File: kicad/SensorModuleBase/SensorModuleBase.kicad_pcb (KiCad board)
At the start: 2 copper layers, 59 x 57 mm, 6 parts, among them J1 Conn_02x08_Top_Bottom, U1 AT28C64B-15PU, U2 74HC00, U3 SN74HC595N, U4 SN74HC595N

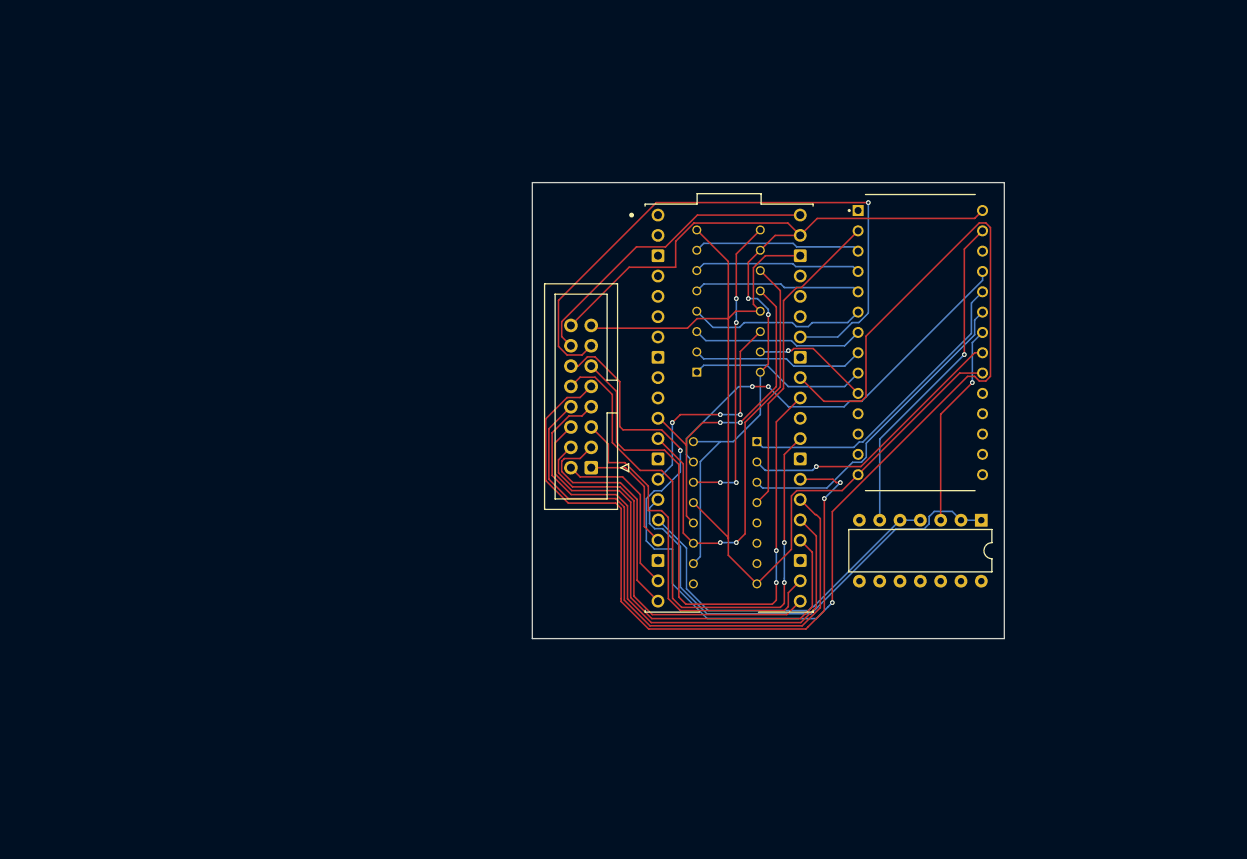
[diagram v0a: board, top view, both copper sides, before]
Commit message: added some kicad files and fixed circuit
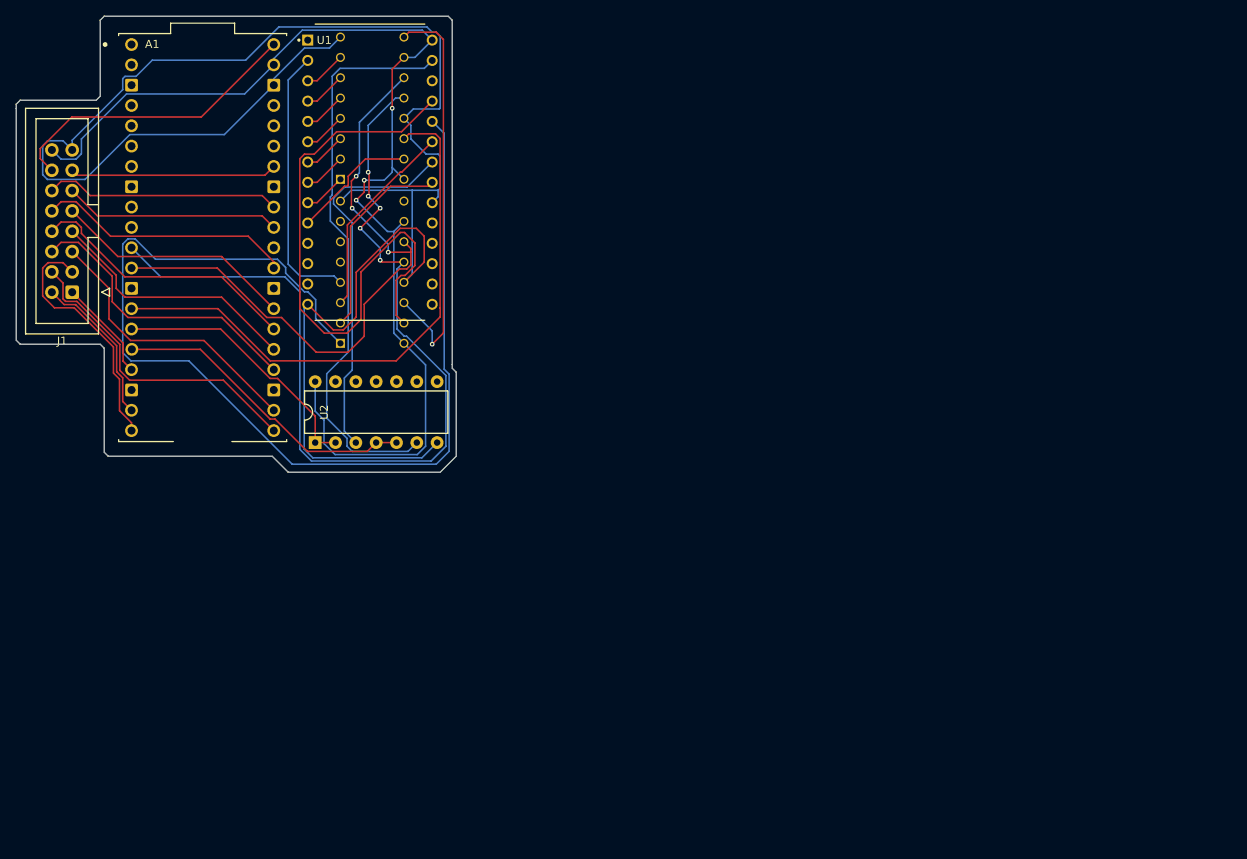
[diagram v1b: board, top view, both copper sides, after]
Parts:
- moved U2 83.8 mm to (52.9, 67.5), turned to 90 degrees
- moved U1 72.0 mm to (59.7, 33.7)
- moved A1 69.2 mm to (38.8, 41.9)
- moved J1 68.5 mm to (22.5, 48.7)
- moved U4 53.4 mm to (60.0, 46.2), turned to 0 degrees
- moved U3 50.7 mm to (60.0, 25.7)
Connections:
- U2 pad 14: (no net) -> Net-(A1-VSYS)
- U2 pad 7: (no net) -> Net-(J1-Pin_15)
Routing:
- net Net-(A1-GP27): track 162.8 -> 29.5 mm, vias 2 -> 0
- net Net-(U1-A9): track 38.8 -> 137.6 mm
- net Net-(J1-Pin_15): track 131.1 -> 228.3 mm
- net Net-(A1-GP8): track 42.6 -> 117.3 mm, vias 2 -> 5
- net Net-(A1-GP21): track 87.4 -> 30.3 mm, vias 2 -> 0
- net Net-(A1-GP28): track 78.1 -> 25.9 mm, vias 1 -> 0
- net Net-(A1-GP26): track 75.6 -> 27.1 mm, vias 2 -> 0
- net Net-(A1-GP10): track 28.2 -> 70.9 mm, vias 3 -> 0
- net Net-(A1-GP22): track 72.8 -> 32.1 mm, vias 2 -> 0
- net Net-(A1-GP20): track 74.1 -> 34.2 mm
- net Net-(A1-GP19): track 71.6 -> 32.3 mm
- net Net-(U1-~{WE}): track 41.5 -> 72.2 mm, vias 1 -> 0
- net Net-(A1-VSYS): track 116.0 -> 143.5 mm, vias 2 -> 3
- net Net-(A1-GP18): track 62.8 -> 36.7 mm
- net Net-(A1-GP11): track 58.9 -> 33.3 mm
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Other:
- board size 59 x 57 mm -> 55 x 57 mm

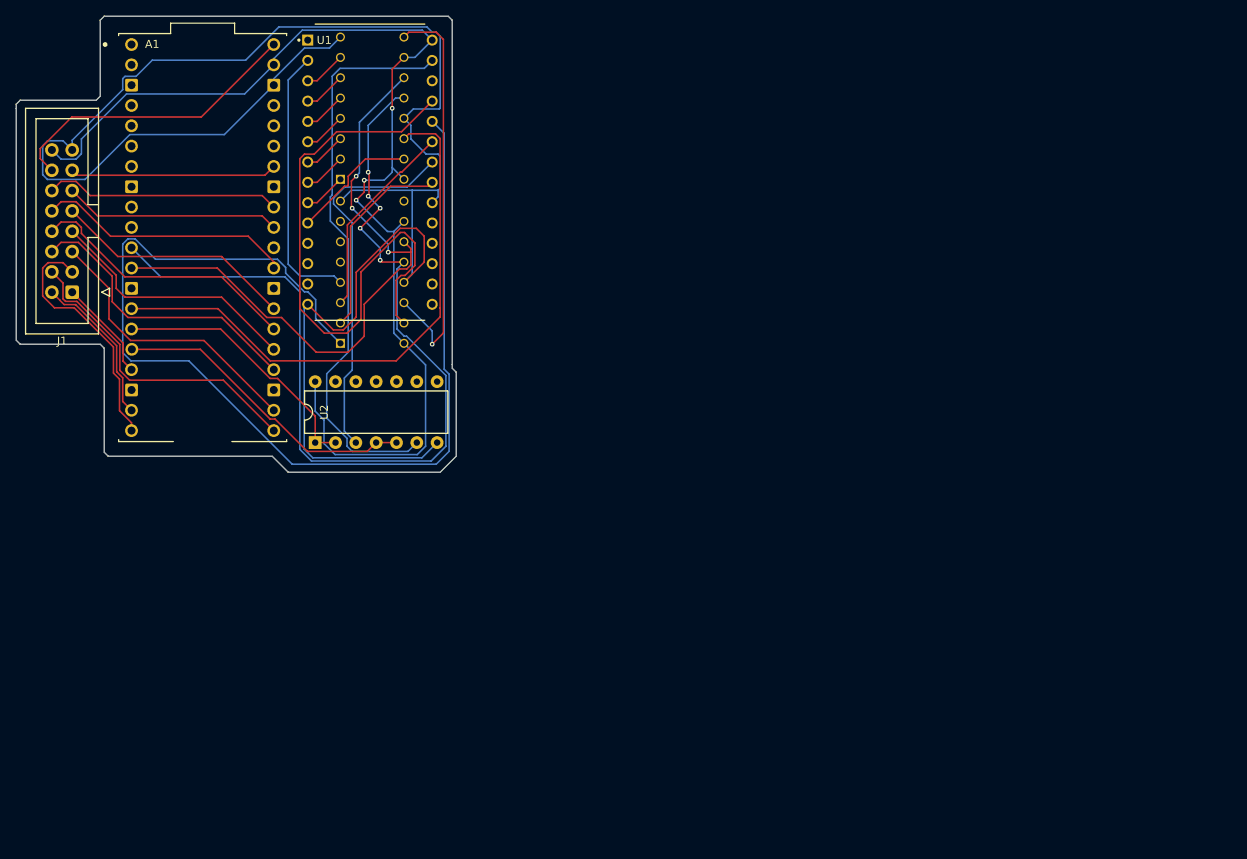
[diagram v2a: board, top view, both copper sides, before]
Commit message: Major progress on Serial, KiCAD models, and Python libraries for sensor module base.
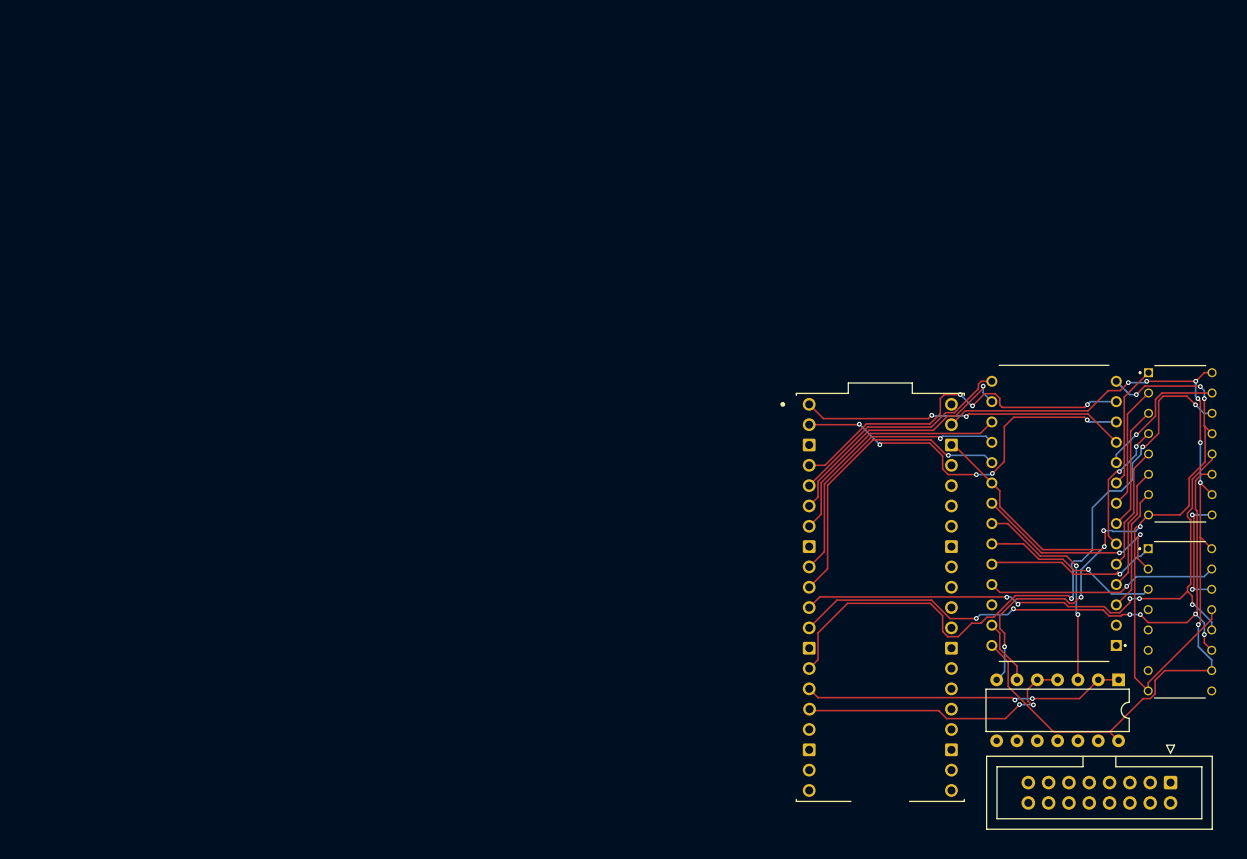
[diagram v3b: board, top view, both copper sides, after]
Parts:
- U3, U4: moved to F.Cu
- moved J1 150.4 mm to (159.8, 110.0), turned to -90 degrees
- moved U4 109.9 mm to (161.0, 89.7)
- moved U3 109.4 mm to (161.0, 67.7)
- moved U2 104.7 mm to (153.3, 97.2), turned to -90 degrees
- moved A1 95.9 mm to (123.5, 86.8)
- moved U1 95.6 mm to (145.2, 76.3), turned to 180 degrees
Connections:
- A1 pad 1: unconnected-(A1-GP0-Pad1) -> Net-(A1-GP0)
- A1 pad 10: unconnected-(A1-GP7-Pad10) -> Net-(A1-GP7)
- A1 pad 2: unconnected-(A1-GP1-Pad2) -> Net-(A1-GP1)
- A1 pad 37: unconnected-(A1-3V3_EN-Pad37) -> Net-(A1-3V3_EN)
- A1 pad 4: unconnected-(A1-GP2-Pad4) -> Net-(A1-GP2)
- A1 pad 40: Net-(A1-VBUS) -> unconnected-(A1-VBUS-Pad40)
- A1 pad 5: unconnected-(A1-GP3-Pad5) -> Net-(A1-GP3)
- A1 pad 6: unconnected-(A1-GP4-Pad6) -> Net-(A1-GP4)
- A1 pad 7: unconnected-(A1-GP5-Pad7) -> Net-(A1-GP5)
- A1 pad 9: unconnected-(A1-GP6-Pad9) -> Net-(A1-GP6)
- J1 pad 14: Net-(A1-VBUS) -> Net-(A1-3V3_EN)
- U1 pad 11: unconnected-(U1-I/O0-Pad11) -> Net-(A1-GP0)
- U1 pad 12: unconnected-(U1-I/O1-Pad12) -> Net-(A1-GP1)
- U1 pad 13: unconnected-(U1-I/O2-Pad13) -> Net-(A1-GP2)
- U1 pad 15: unconnected-(U1-I/O3-Pad15) -> Net-(A1-GP3)
- U1 pad 16: unconnected-(U1-I/O4-Pad16) -> Net-(A1-GP4)
- U1 pad 17: unconnected-(U1-I/O5-Pad17) -> Net-(A1-GP5)
- U1 pad 18: unconnected-(U1-I/O6-Pad18) -> Net-(A1-GP6)
- U1 pad 19: unconnected-(U1-I/O7-Pad19) -> Net-(A1-GP7)
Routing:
- net Net-(U1-A9): track 137.6 -> 21.8 mm, vias 0 -> 1
- net Net-(J1-Pin_15): track 228.3 -> 132.8 mm, vias 0 -> 8
- net Net-(U1-~{WE}): track 72.2 -> 8.14 mm
- net Net-(A1-GP1): track 0.00 -> 47.9 mm, vias 0 -> 5
- net Net-(A1-GP2): track 0.00 -> 45.8 mm, vias 0 -> 3
- net Net-(U1-A8): track 74.8 -> 29.1 mm, vias 0 -> 1
- net Net-(A1-GP8): track 117.3 -> 75.3 mm
- net Net-(A1-GP0): track 0.00 -> 41.0 mm, vias 0 -> 2
- net Net-(A1-GP16): track 39.0 -> 0.00 mm
- net Net-(A1-VBUS): track 37.9 -> 0.00 mm
- net Net-(A1-GP7): track 0.00 -> 37.8 mm, vias 0 -> 1
- net Net-(A1-GP18): track 36.7 -> 0.00 mm
- net Net-(U3-QH'): track 50.9 -> 14.4 mm, vias 1 -> 2
- net Net-(A1-GP17): track 35.7 -> 0.00 mm
- net Net-(A1-GP6): track 0.00 -> 35.1 mm, vias 0 -> 1
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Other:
- board outline removed

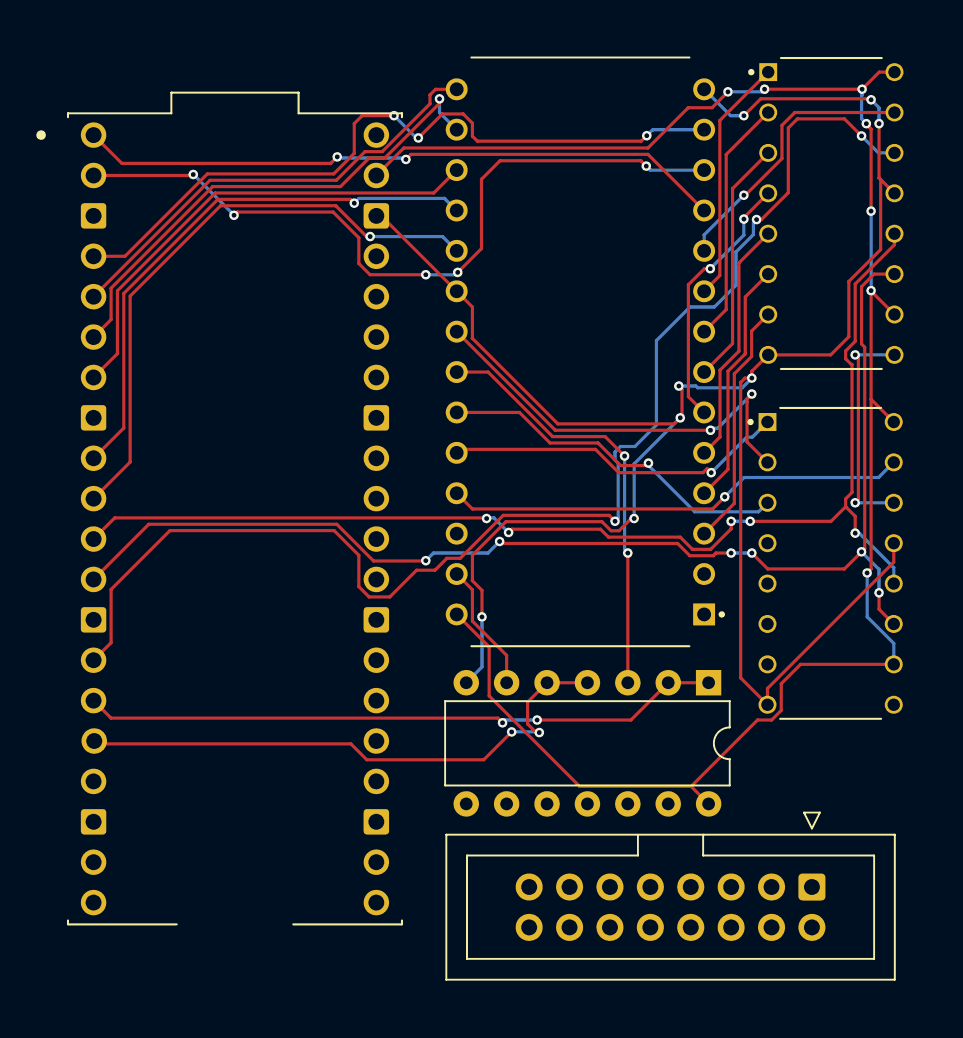
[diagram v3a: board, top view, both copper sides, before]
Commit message: Finished new Sensor Base KiCAD module and working on serial pairing.
Serial pairing issue: deadlock between cores due to core1 failing to read data from std::cin.
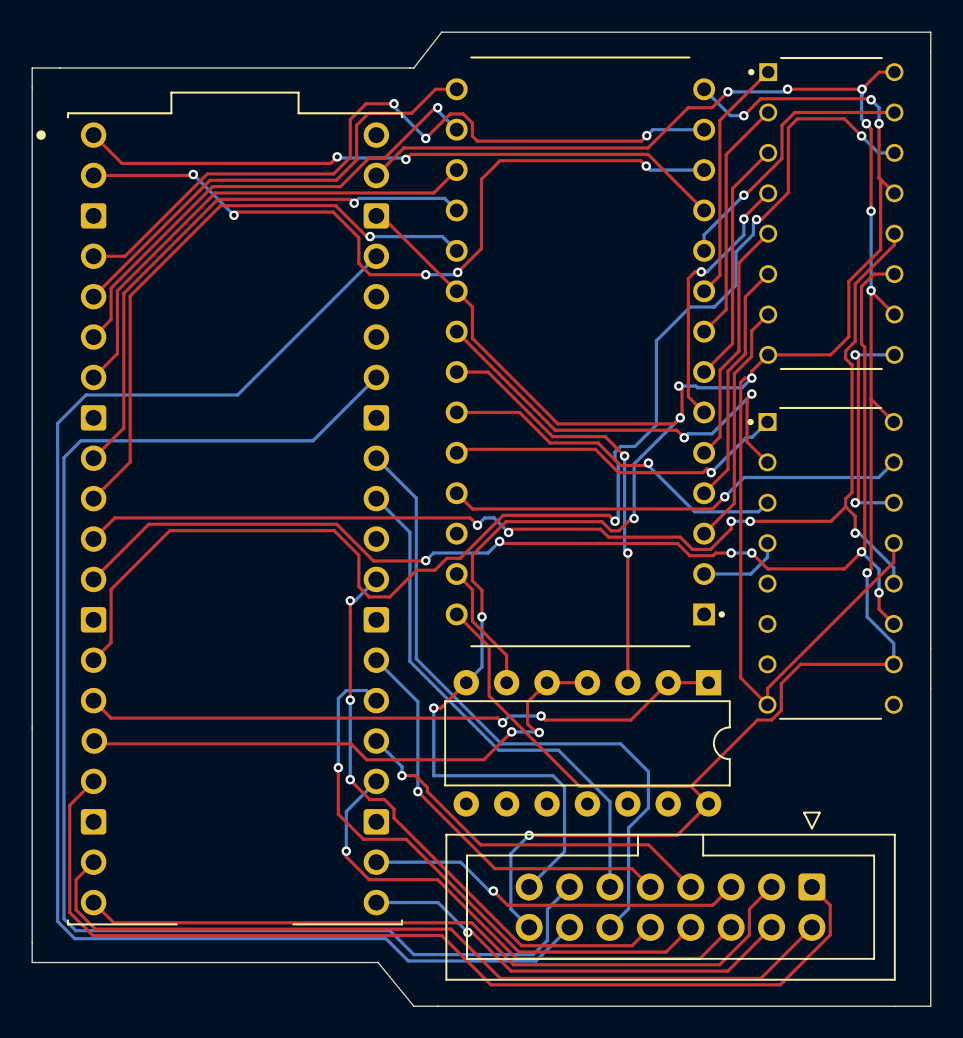
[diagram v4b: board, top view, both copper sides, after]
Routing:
- net Net-(A1-3V3_EN): track 0.00 -> 89.8 mm
- net Net-(A1-GP28): track 0.00 -> 86.4 mm
- net Net-(A1-GP13): track 0.00 -> 63.4 mm
- net Net-(A1-GP14): track 0.00 -> 52.8 mm
- net Net-(A1-GP15): track 0.00 -> 47.2 mm
- net Net-(A1-GP27): track 0.00 -> 42.0 mm
- net Net-(A1-GP22): track 0.00 -> 37.5 mm, vias 0 -> 3
- net Net-(A1-GP20): track 0.00 -> 36.5 mm, vias 0 -> 1
- net Net-(A1-GP18): track 0.00 -> 33.2 mm, vias 0 -> 1
- net Net-(A1-GP26): track 0.00 -> 32.7 mm
- net Net-(A1-GP16): track 0.00 -> 27.8 mm, vias 0 -> 1
- net Net-(A1-GP21): track 0.00 -> 26.4 mm, vias 0 -> 1
- net Net-(A1-GP19): track 0.00 -> 24.1 mm, vias 0 -> 1
- net Net-(A1-GP17): track 0.00 -> 23.9 mm, vias 0 -> 1
- net Net-(J1-Pin_15): track 132.8 -> 155.4 mm, vias 8 -> 9
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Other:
- board outline added: 56.5 x 61.2 mm
